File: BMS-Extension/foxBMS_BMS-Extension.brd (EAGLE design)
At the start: 156 x 120 mm, 223 parts, among them IC1001 AQV252G2S, IC1002 AQV252G2S, IC1003 AQV252G2S, IC1101 UA78L05ACPK, IC1102 ADUM1300ARW, IC1301 UA78L05ACPK, IC1302 LTC485CS8#PBF, IC1303 ADUM1401ARW, IC1701 ADR3425ARJZ, IC1901 UA78L05ACPK, IC1902 ADUM1402ARW, IC1903 ADUM1402ARW, IC2001 AQV25G2S, IC2002 AQV25G2S, IC2003 AQV25G2S, IC2004 AQV25G2S, IC2005 AQV25G2S, IC2006 AQV25G2S, IC801 KA7805ERTF, IC802 CPC1008N, IC803 TJA1052IT/1Y, T1001 IRLML0100TRPBF, T1002 IRLML0100TRPBF, T1003 IRLML0100TRPBF, T1501 BSS84P, T2001 IRLML0100TRPBF, T2002 IRLML0100TRPBF, T2003 IRLML0100TRPBF, T2004 IRLML0100TRPBF, T2005 IRLML0100TRPBF, T2006 IRLML0100TRPBF, T801 IRLML0100TRPBF, T901 BUK964R8-60E, X1201 43045-0400_MOLEX_4PIN, X1202 43045-0400_MOLEX_4PIN, X1203 43045-0400_MOLEX_4PIN, X1301 43045-0600_MOLEX_6PIN, X1701 43045-1200_MOLEX_12PIN, X1901 43045-1000_MOLEX_10PIN, X2001 43045-1200_MOLEX_12PIN, X801 43045-0400_MOLEX_4PIN

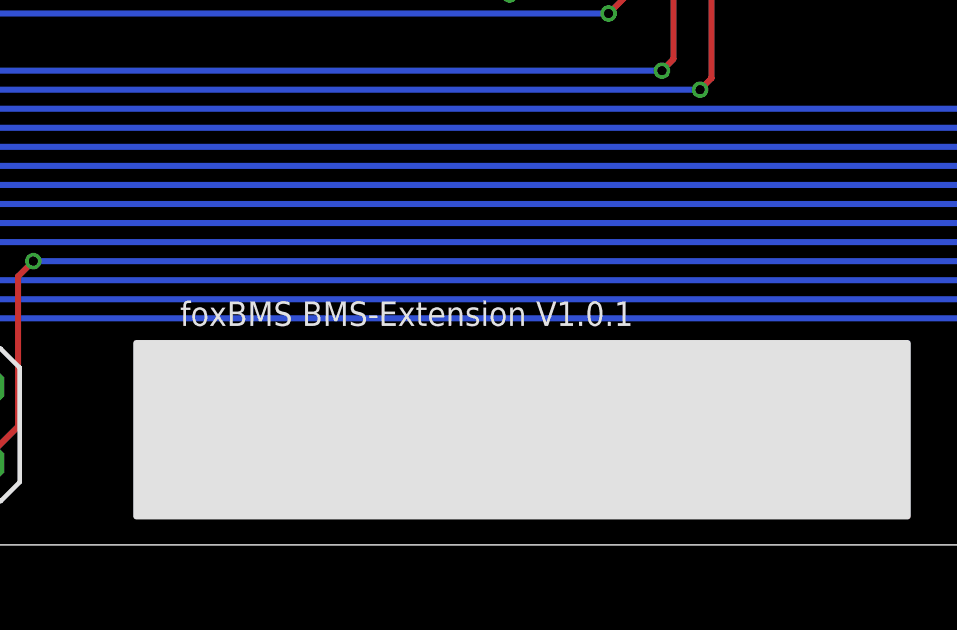
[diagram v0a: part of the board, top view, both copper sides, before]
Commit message: Changed ADUM1xxx to ADUM3xxx in schematic of BMS-Master and BMS-Extension
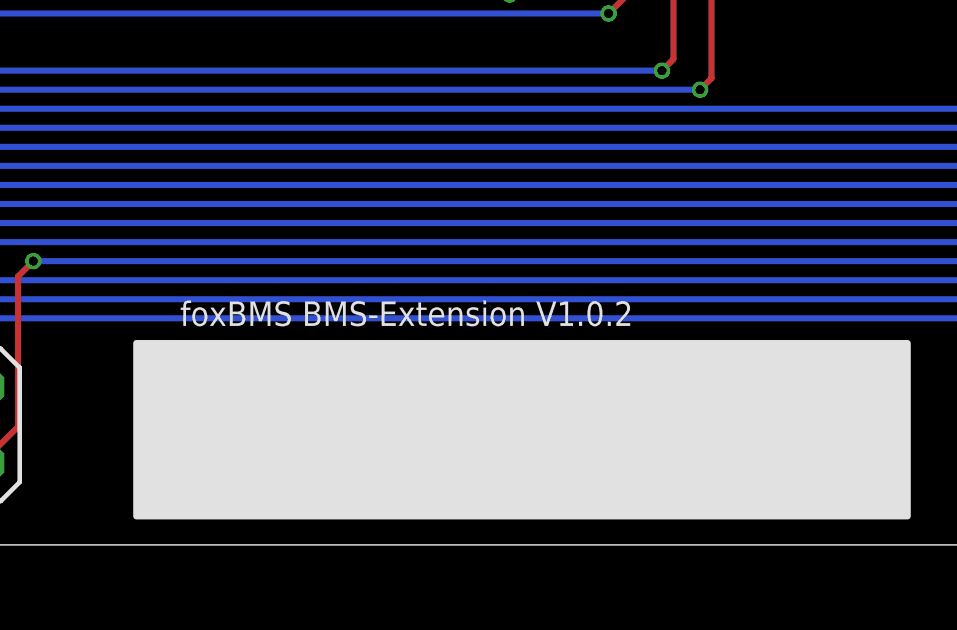
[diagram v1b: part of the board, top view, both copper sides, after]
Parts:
- IC1102: value ADUM1300ARW -> ADUM3300ARW; device 0_LES_SCHNITTSTELLEN-IC.SMD.ISOLATOR:IC_SMD_SOIC-16_(JEDEC_MS-013-AA)_R_ANALOG_REV01 -> foxBMS_BMS-Master:IC_SMD_SOIC-16_(JEDEC_MS-013-AA)_R_ANALOG_REV01
- IC1303: value ADUM1401ARW -> ADUM3401ARW; device 0_LES_SCHNITTSTELLEN-IC.SMD.ISOLATOR:IC_SMD_SOIC-16_(JEDEC_MS-013-AA)_R_ANALOG_REV01 -> foxBMS_BMS-Master:IC_SMD_SOIC-16_(JEDEC_MS-013-AA)_R_ANALOG_REV01
- IC1902, IC1903: value ADUM1402ARW -> ADUM3402ARW; device 0_LES_SCHNITTSTELLEN-IC.SMD.ISOLATOR:IC_SMD_SOIC-16_(JEDEC_MS-013-AA)_R_ANALOG_REV01 -> foxBMS_BMS-Extension:IC_SMD_SOIC-16_(JEDEC_MS-013-AA)_R_ANALOG_REV01
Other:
- board text added: "foxBMS BMS-Extension V1.0.2"
- board text removed: "foxBMS BMS-Extension V1.0.1"

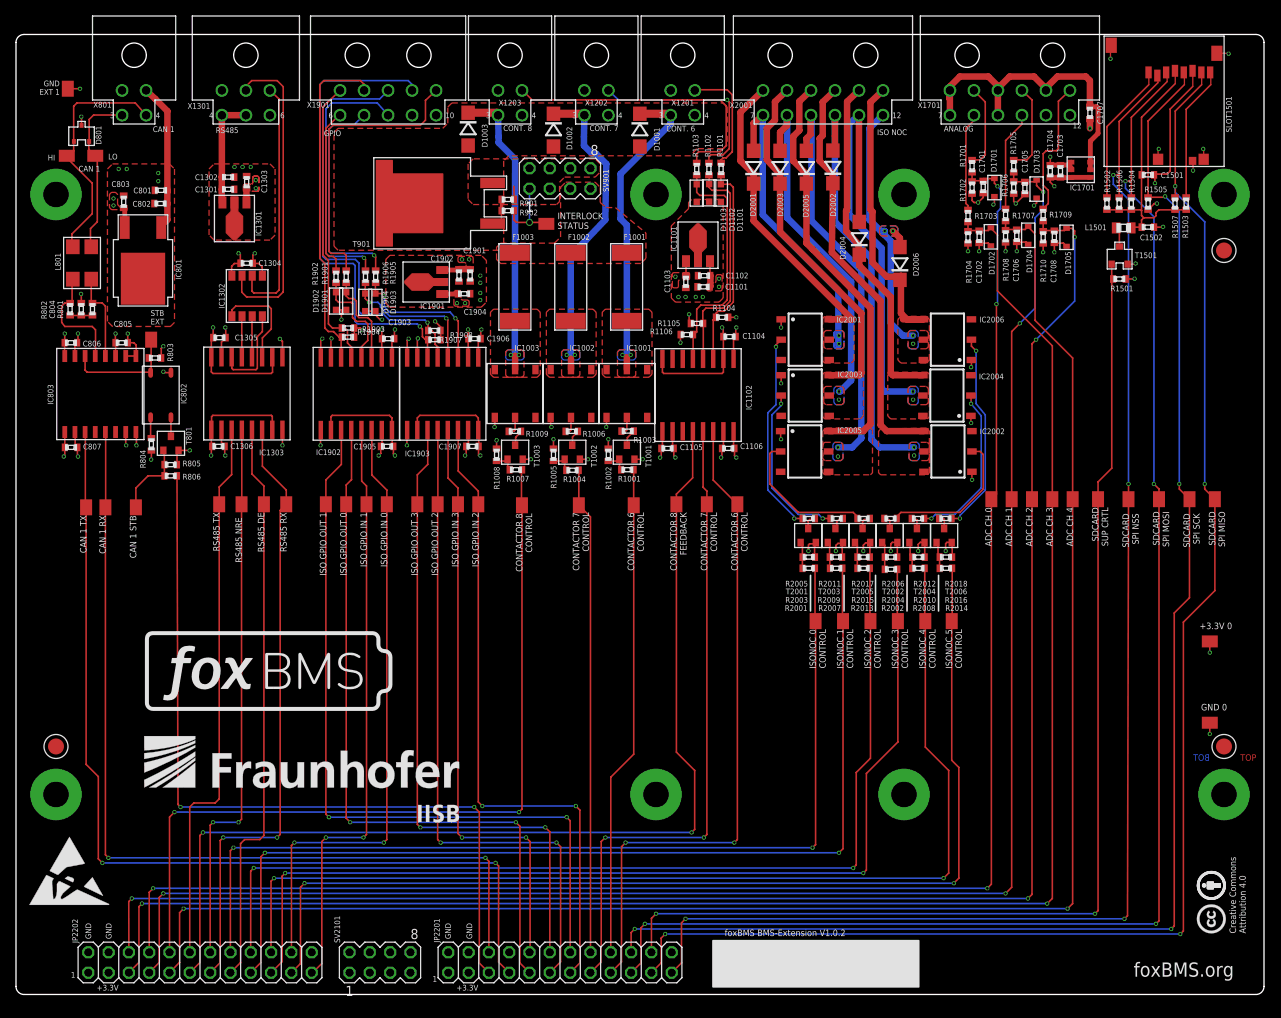
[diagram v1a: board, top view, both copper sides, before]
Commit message: updated foxBMS-slave to version 2.02
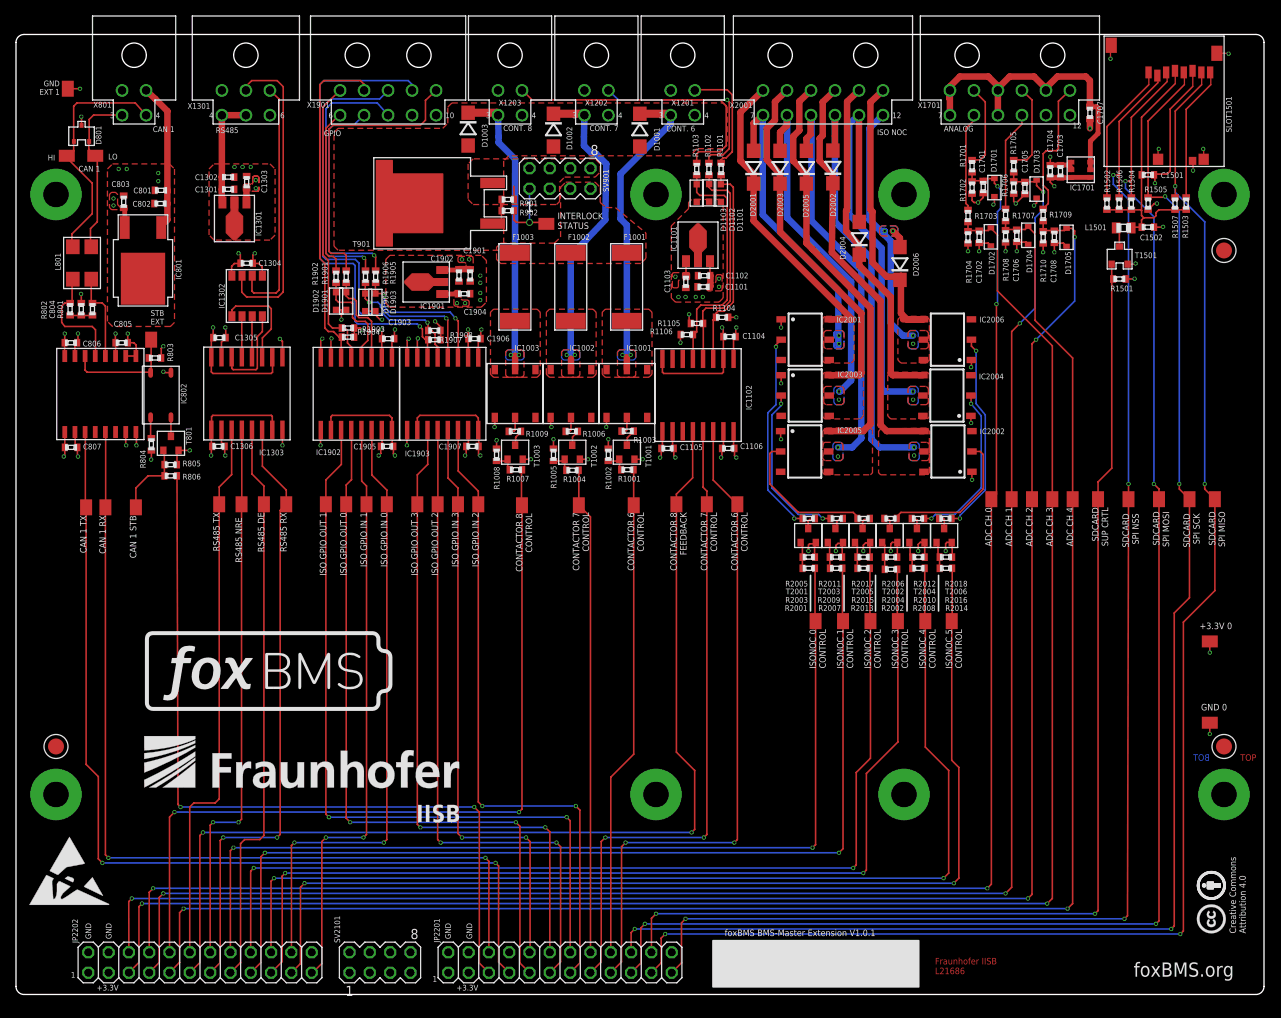
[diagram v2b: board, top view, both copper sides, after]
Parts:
- IC1102: value ADUM3300ARW -> ADUM1300ARW; device foxBMS_BMS-Master:IC_SMD_SOIC-16_(JEDEC_MS-013-AA)_R_ANALOG_REV01 -> 0_LES_SCHNITTSTELLEN-IC.SMD.ISOLATOR:IC_SMD_SOIC-16_(JEDEC_MS-013-AA)_R_ANALOG_REV01
- IC1303: value ADUM3401ARW -> ADUM1401ARW; device foxBMS_BMS-Master:IC_SMD_SOIC-16_(JEDEC_MS-013-AA)_R_ANALOG_REV01 -> 0_LES_SCHNITTSTELLEN-IC.SMD.ISOLATOR:IC_SMD_SOIC-16_(JEDEC_MS-013-AA)_R_ANALOG_REV01
- IC1902, IC1903: value ADUM3402ARW -> ADUM1402ARW; device foxBMS_BMS-Extension:IC_SMD_SOIC-16_(JEDEC_MS-013-AA)_R_ANALOG_REV01 -> 0_LES_SCHNITTSTELLEN-IC.SMD.ISOLATOR:IC_SMD_SOIC-16_(JEDEC_MS-013-AA)_R_ANALOG_REV01
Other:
- board text added: "Fraunhofer IISB L21686"
- board text added: "foxBMS BMS-Master Extension V1.0.1"
- board text removed: "foxBMS BMS-Extension V1.0.2"
